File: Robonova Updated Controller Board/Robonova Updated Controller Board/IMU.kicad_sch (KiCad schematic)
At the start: 25 parts

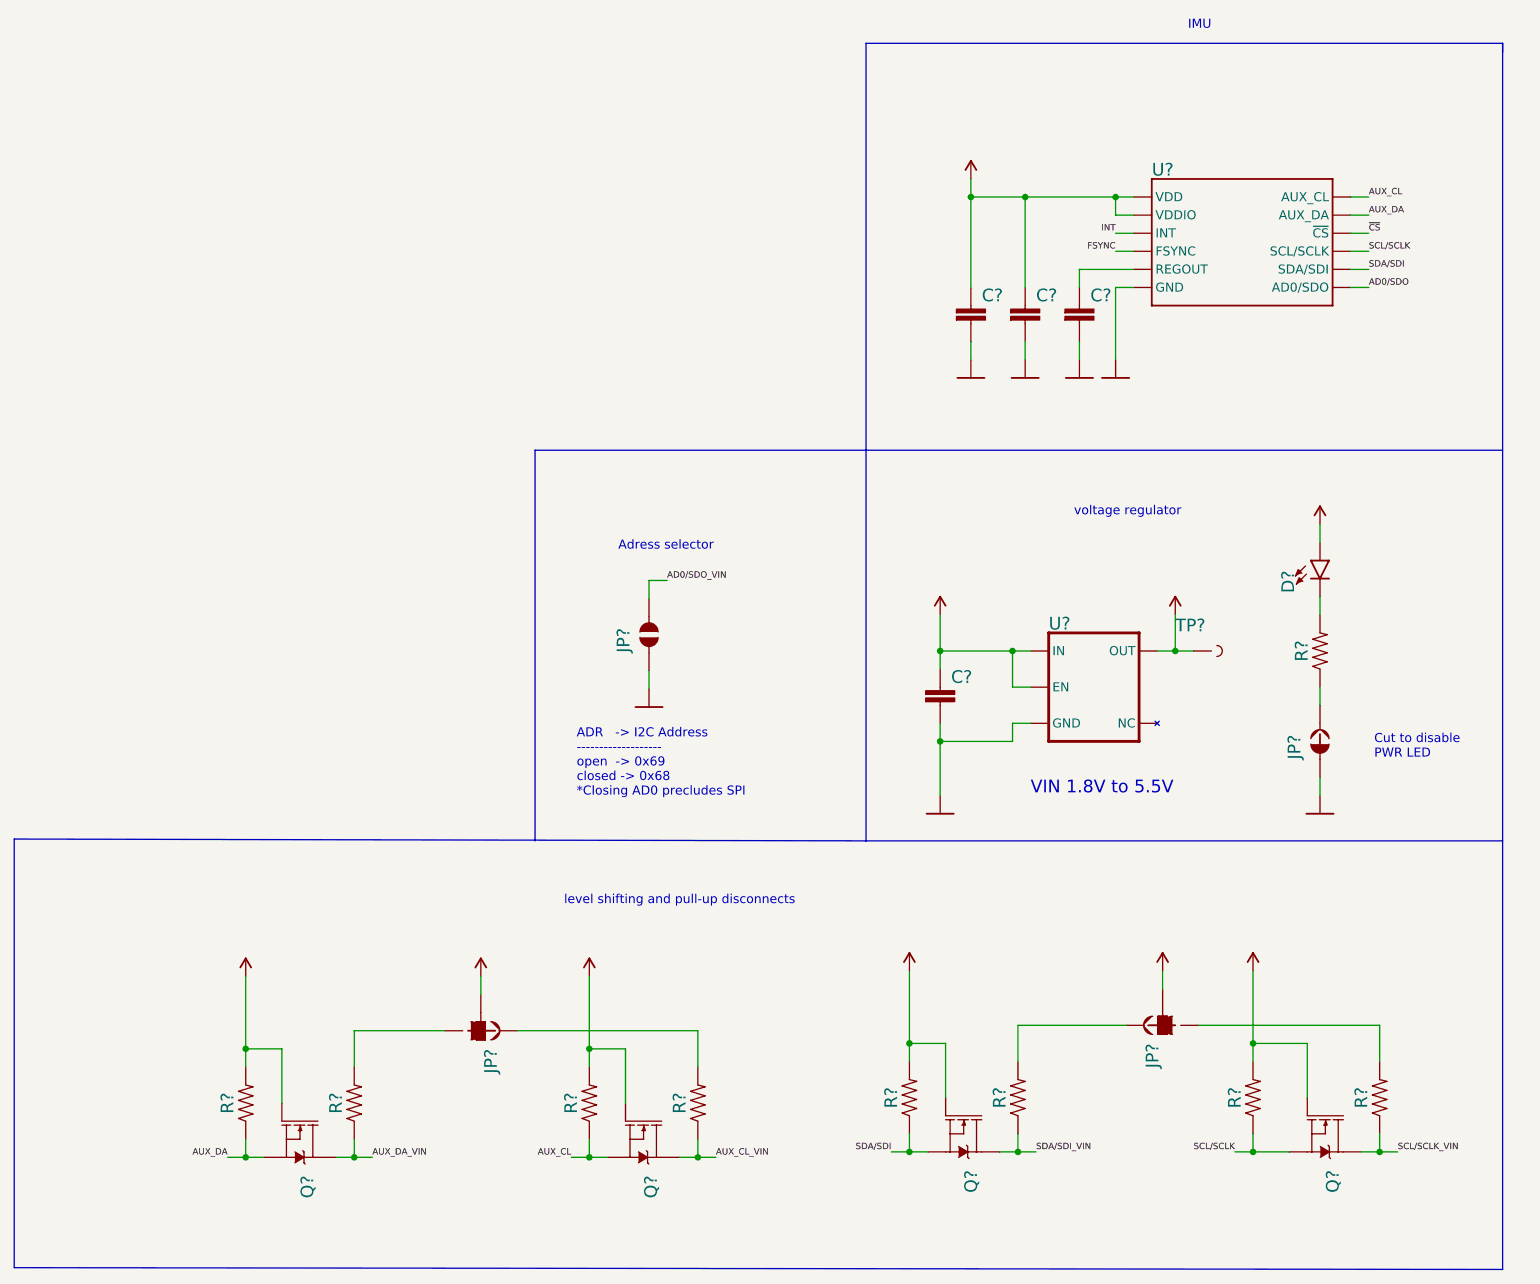
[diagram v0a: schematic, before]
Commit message: Removed useless files and added some libraries to kicad
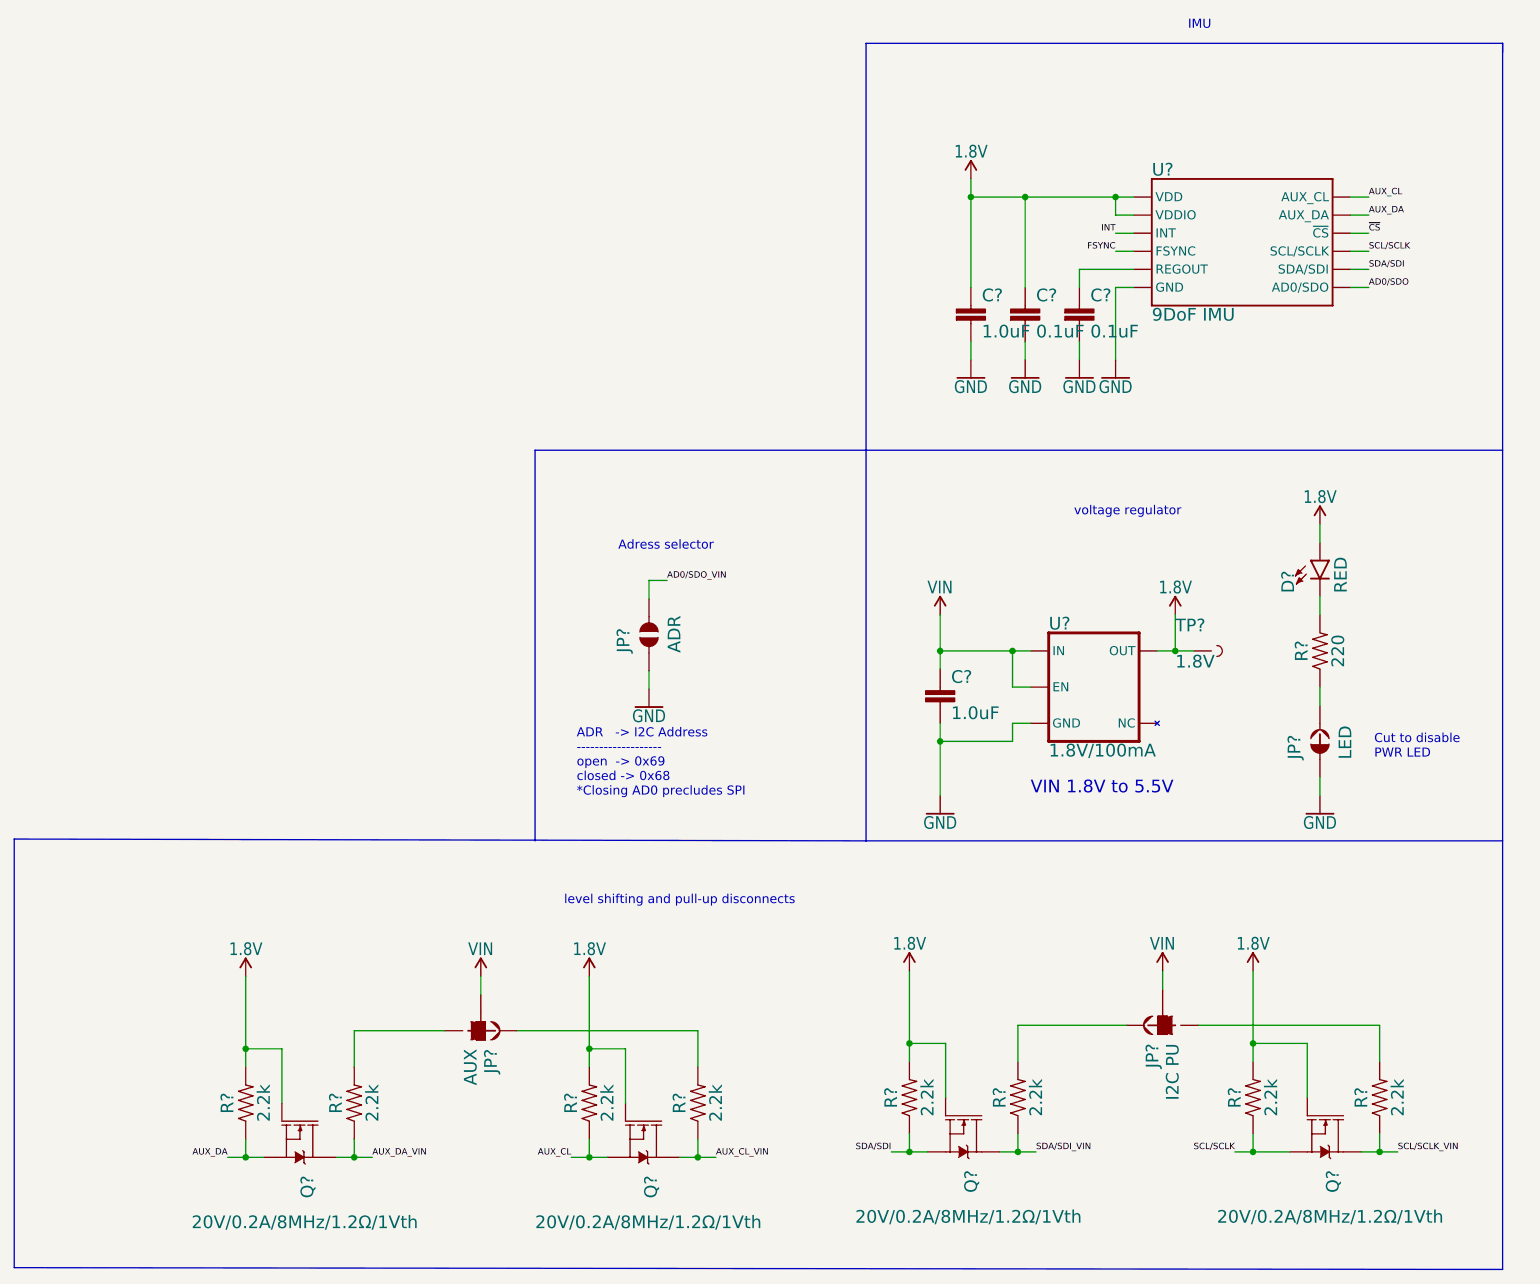
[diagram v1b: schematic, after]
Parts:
- C? (x2): value (none) -> 1.0uF; footprint (none) -> Robonova Updated Controller Board:0603
- C? (x2): value (none) -> 0.1uF; footprint (none) -> Robonova Updated Controller Board:0603
- D?: value (none) -> RED; footprint (none) -> Robonova Updated Controller Board:LED-0603
- JP?: value (none) -> ADR; footprint (none) -> Robonova Updated Controller Board:SMT-JUMPER_2_NO_SILK
- JP?: value (none) -> LED; footprint (none) -> Robonova Updated Controller Board:SMT-JUMPER_2_NC_TRACE_SILK
- JP?: value (none) -> I2C PU; footprint (none) -> Robonova Updated Controller Board:SMT-JUMPER_3_2-NC_TRACE_SILK
- JP?: value (none) -> AUX; footprint (none) -> Robonova Updated Controller Board:SMT-JUMPER_3_2-NC_TRACE_SILK
- Q? (x4): value (none) -> 20V/0.2A/8MHz/1.2Ω/1Vth; footprint (none) -> Robonova Updated Controller Board:SOT-416FL
- R? (x8): value (none) -> 2.2k; footprint (none) -> Robonova Updated Controller Board:0402-TIGHT
- R?: value (none) -> 220; footprint (none) -> Robonova Updated Controller Board:0603
- TP?: value (none) -> 1.8V; footprint (none) -> Robonova Updated Controller Board:PAD.03X.03
- U?: value (none) -> 9DoF IMU; footprint (none) -> Robonova Updated Controller Board:QFN24-3X3
- U?: value (none) -> 1.8V/100mA; footprint (none) -> Robonova Updated Controller Board:SC70
